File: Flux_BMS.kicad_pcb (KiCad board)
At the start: 4 copper layers, 100 x 100 mm, 151 parts, among them J1 Conn_01x13, J2 CAN, J3 Conn_01x02, J4 Conn_01x05, J5 USB_C_Receptacle_USB2.0, J6 Conn_01x02, J7 Conn_01x05, Q1 BSS84, Q10 BSS84, Q11 BSS84, Q12 BSS84, Q13 Q_NMOS_SDG, Q14 Q_NMOS_SDG, Q2 BSS84, Q3 BSS84, Q4 BSS84, Q5 BSS84, Q6 BSS84, Q7 BSS84, Q8 BSS84, Q9 BSS84, U1 LTC6811-1, U2 STM32L476RGTx, U3 BQ76200PW, U4 TJA1051T-3, U7 SY8502, U8 SE8533, U9 INA180A2, X1 8MHz(16pF)

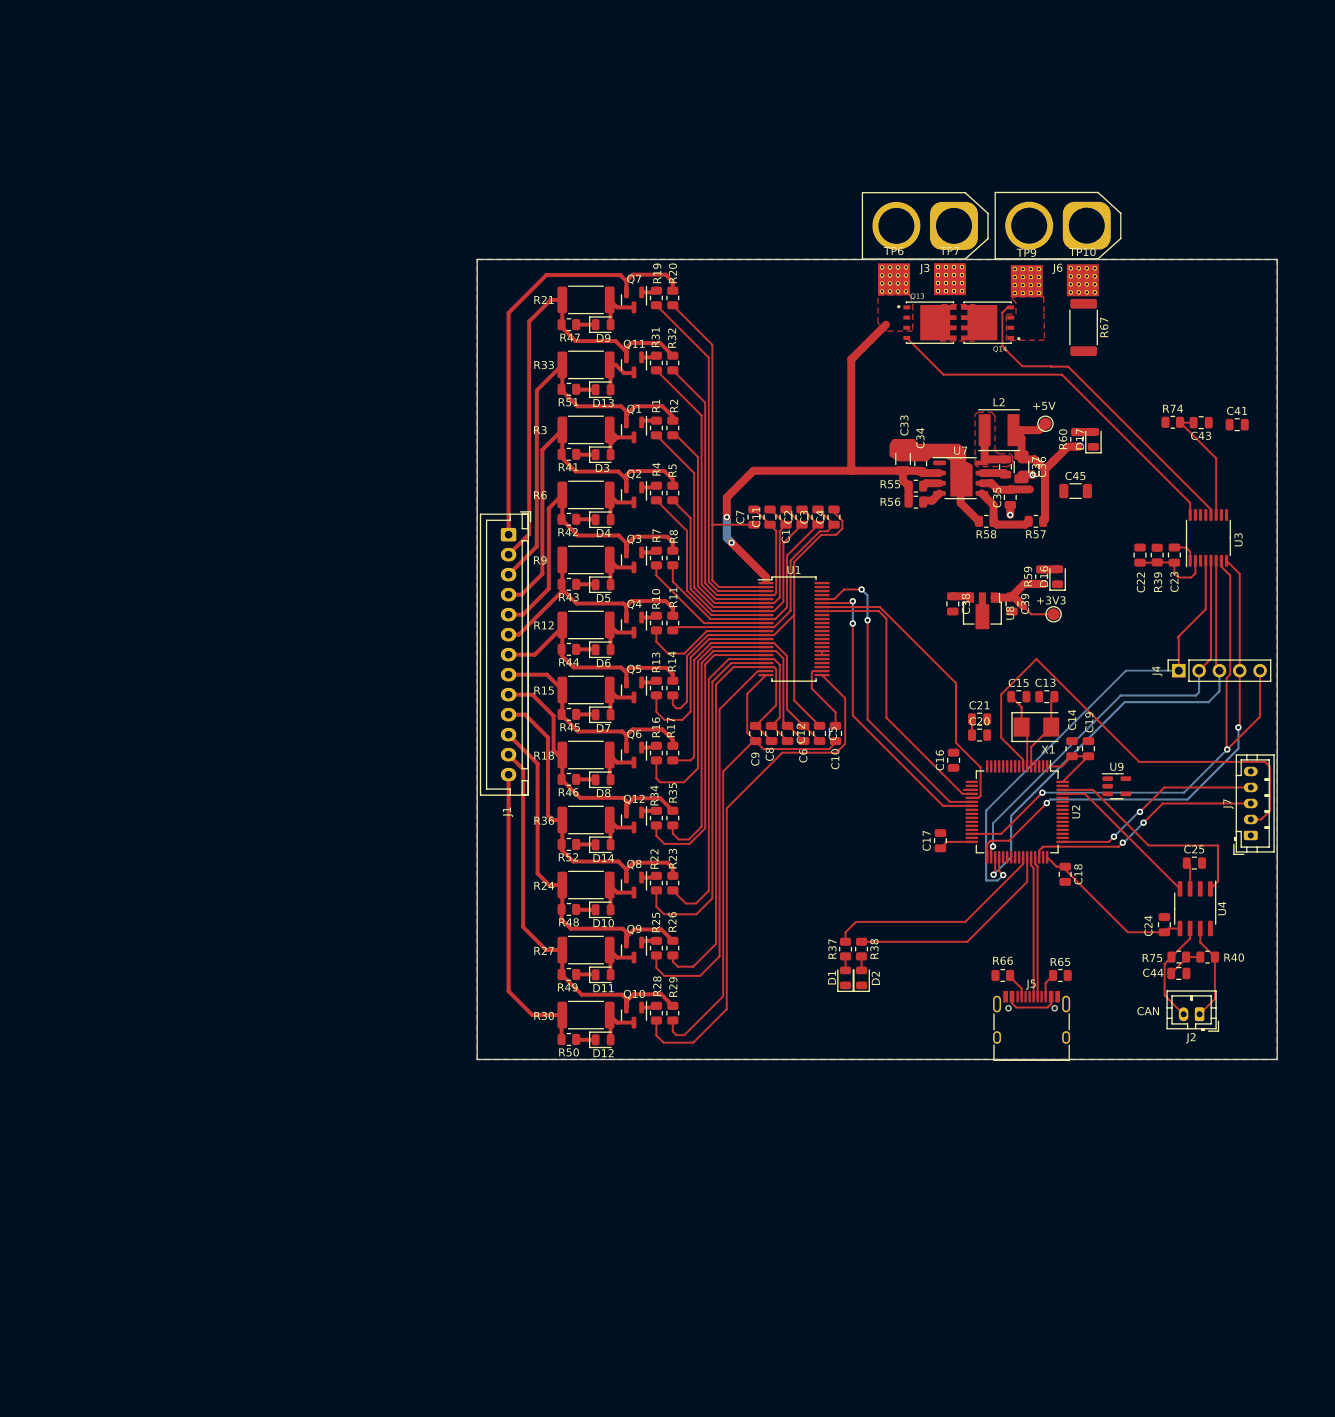
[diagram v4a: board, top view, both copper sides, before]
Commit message: new board dimensions
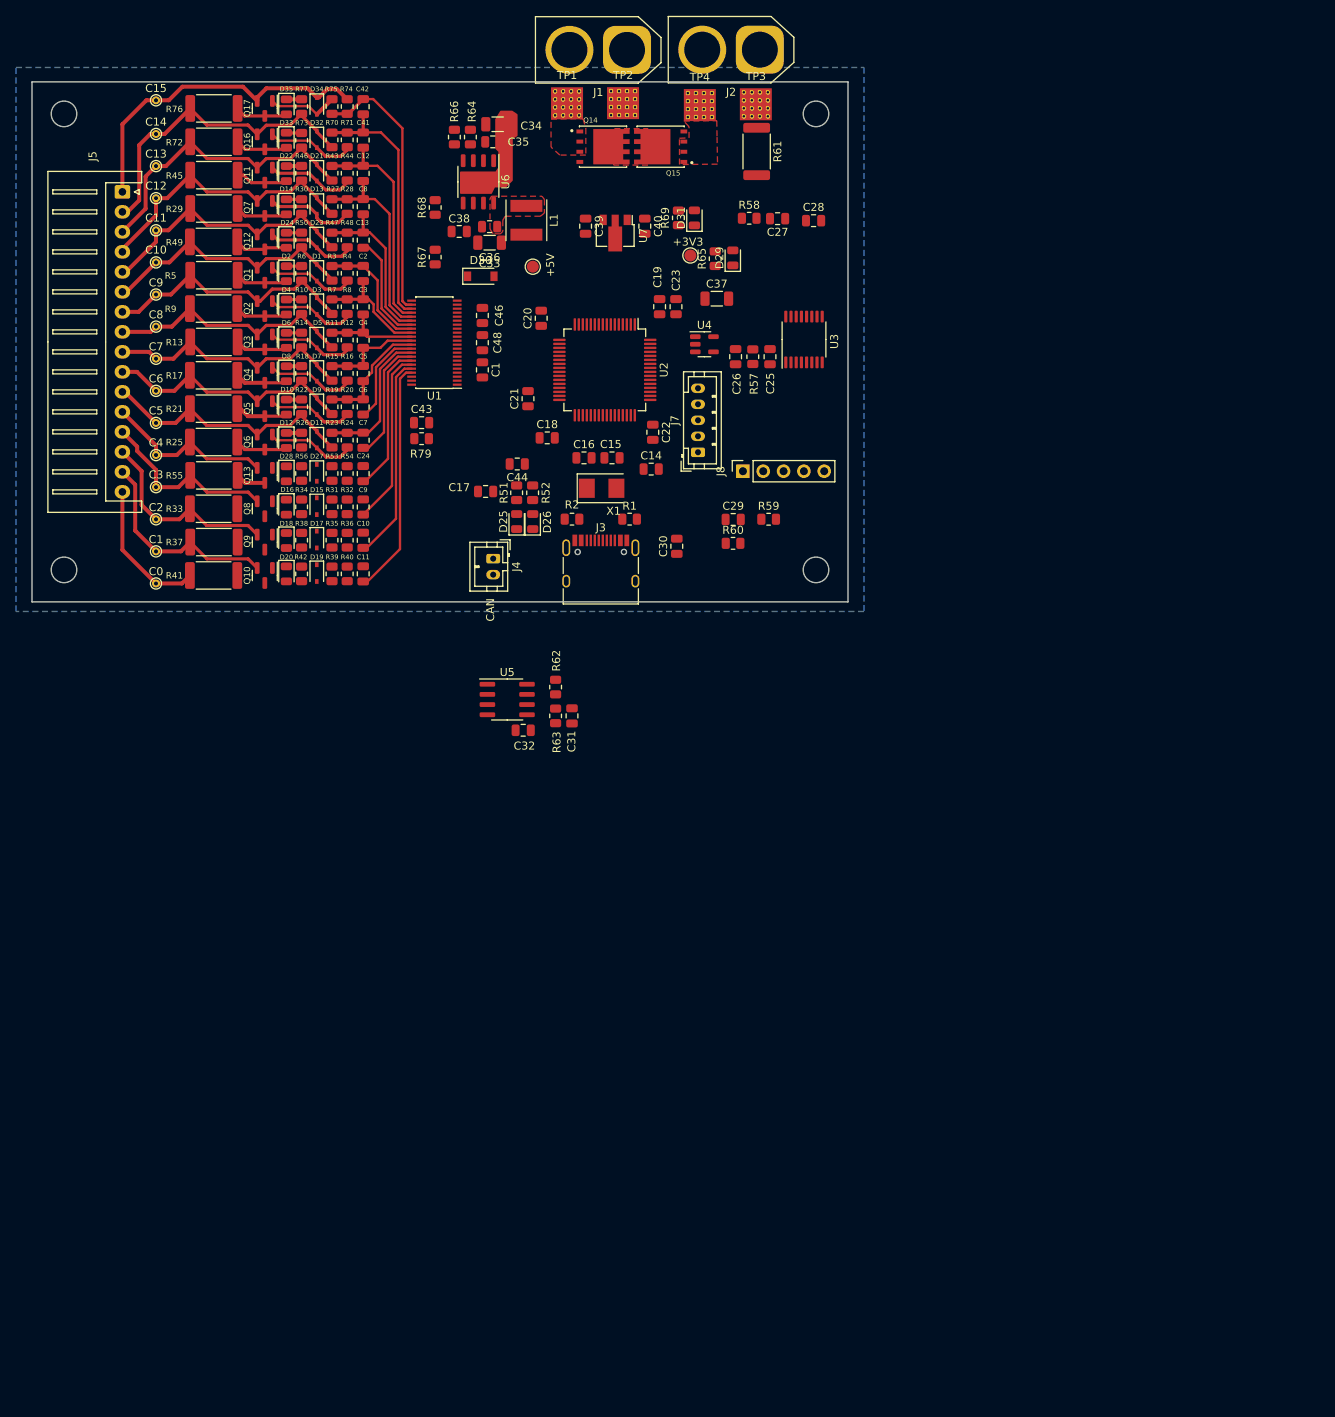
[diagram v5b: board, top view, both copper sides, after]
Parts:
- removed the J1 at (78.9, 84.4)
- removed the R1 at (97.4, 71.1)
- removed the R2 at (99.5, 71.1)
- removed the R51 at (86.5, 66.2)
- removed the R52 at (86.5, 123.1)
- added C13: ~, Capacitor_SMD:C_0805_2012Metric, F.Cu at (60.8, 47.6)
- added C14: C, Capacitor_SMD:C_0805_2012Metric, F.Cu at (96.8, 76.2)
- added C24: ~, Capacitor_SMD:C_0805_2012Metric, F.Cu at (60.8, 76.8)
- added C29: 100n, Capacitor_SMD:C_0805_2012Metric, F.Cu at (107.0, 82.5)
- added C41: ~, Capacitor_SMD:C_0805_2012Metric, F.Cu at (60.8, 35.1)
- added C42: ~, Capacitor_SMD:C_0805_2012Metric, F.Cu at (60.8, 30.9)
- added C43: 470p, Capacitor_SMD:C_0805_2012Metric, F.Cu at (68.0, 70.4)
- added C44: 4u7, Capacitor_SMD:C_0805_2012Metric, F.Cu at (80.0, 75.6)
- added C46: 1u, Capacitor_SMD:C_0805_2012Metric, F.Cu at (75.7, 57.0)
- added C48: 1u, Capacitor_SMD:C_0805_2012Metric, F.Cu at (75.7, 60.4)
- added D1: ~, Diode_SMD:D_SOD-323, F.Cu at (55.0, 51.6)
- added D15: ~, Diode_SMD:D_SOD-323, F.Cu at (55.0, 80.8)
- added D16: RED, LED_SMD:LED_0805_2012Metric, F.Cu at (51.1, 81.0)
- added D17: ~, Diode_SMD:D_SOD-323, F.Cu at (55.0, 85.0)
- added D18: RED, LED_SMD:LED_0805_2012Metric, F.Cu at (51.1, 85.1)
- added D19: ~, Diode_SMD:D_SOD-323, F.Cu at (55.0, 89.2)
- added D2: RED, LED_SMD:LED_0805_2012Metric, F.Cu at (51.1, 51.8)
- added D20: RED, LED_SMD:LED_0805_2012Metric, F.Cu at (51.1, 89.3)
- added D21: ~, Diode_SMD:D_SOD-323, F.Cu at (55.0, 39.1)
- added D22: RED, LED_SMD:LED_0805_2012Metric, F.Cu at (51.1, 39.3)
- added D23: ~, Diode_SMD:D_SOD-323, F.Cu at (55.0, 47.5)
- added D24: RED, LED_SMD:LED_0805_2012Metric, F.Cu at (51.1, 47.6)
- added D27: ~, Diode_SMD:D_SOD-323, F.Cu at (55.0, 76.7)
- added D28: RED, LED_SMD:LED_0805_2012Metric, F.Cu at (51.1, 76.8)
- added D30: D_Schottky, Diode_SMD:D_SOD-123, F.Cu at (75.5, 52.1)
- added D32: ~, Diode_SMD:D_SOD-323, F.Cu at (55.0, 35.0)
- added D33: RED, LED_SMD:LED_0805_2012Metric, F.Cu at (51.1, 35.1)
- added D34: ~, Diode_SMD:D_SOD-323, F.Cu at (55.0, 30.8)
- added D35: RED, LED_SMD:LED_0805_2012Metric, F.Cu at (51.1, 30.9)
- added H1: MountingHole, MountingHole:MountingHole_3.2mm_M3, F.Cu at (23.4, 31.8)
- added H2: MountingHole, MountingHole:MountingHole_3.2mm_M3, F.Cu at (23.4, 88.8)
- added H3: MountingHole, MountingHole:MountingHole_3.2mm_M3, F.Cu at (117.3, 31.8)
- added H4: MountingHole, MountingHole:MountingHole_3.2mm_M3, F.Cu at (117.3, 88.8)
- added J5: Conn_01x16, Connector_JST:JST_XH_S16B-XH-A_1x16_P2.50mm_Horizontal, F.Cu at (30.6, 41.5)
- added Q13: ~, Package_TO_SOT_SMD:SOT-23, F.Cu at (48.5, 77.0)
- added Q16: ~, Package_TO_SOT_SMD:SOT-23, F.Cu at (48.5, 35.3)
- added Q17: ~, Package_TO_SOT_SMD:SOT-23, F.Cu at (48.5, 31.1)
- added R37: 33, Resistor_SMD:R_2512_6332Metric, F.Cu at (42.1, 85.3)
- added R38: 470, Resistor_SMD:R_0805_2012Metric, F.Cu at (53.0, 85.1)
- added R39: 1k, Resistor_SMD:R_0805_2012Metric, F.Cu at (56.9, 89.3)
- added R40: 10k, Resistor_SMD:R_0805_2012Metric, F.Cu at (58.8, 89.3)
- added R53: 1k, Resistor_SMD:R_0805_2012Metric, F.Cu at (56.9, 76.7)
- added R54: 10k, Resistor_SMD:R_0805_2012Metric, F.Cu at (58.8, 76.7)
- added R55: 33, Resistor_SMD:R_2512_6332Metric, F.Cu at (42.1, 77.0)
- added R56: 470, Resistor_SMD:R_0805_2012Metric, F.Cu at (53.0, 76.7)
- added R59: 470k (was 520k), Resistor_SMD:R_0805_2012Metric, F.Cu at (111.4, 82.5)
- added R60: 10k, Resistor_SMD:R_0805_2012Metric, F.Cu at (107.0, 85.5)
- added R70: 1k, Resistor_SMD:R_0805_2012Metric, F.Cu at (56.9, 35.1)
- added R71: 10k, Resistor_SMD:R_0805_2012Metric, F.Cu at (58.8, 35.1)
- added R72: 33, Resistor_SMD:R_2512_6332Metric, F.Cu at (42.1, 35.3)
- added R73: 470, Resistor_SMD:R_0805_2012Metric, F.Cu at (53.0, 35.1)
- added R74: 1k, Resistor_SMD:R_0805_2012Metric, F.Cu at (58.8, 30.9)
- added R75: 10k, Resistor_SMD:R_0805_2012Metric, F.Cu at (56.9, 30.9)
- added R76: 33, Resistor_SMD:R_2512_6332Metric, F.Cu at (42.1, 31.1)
- added R77: 470, Resistor_SMD:R_0805_2012Metric, F.Cu at (53.0, 30.9)
- added R79: 499k, Resistor_SMD:R_0805_2012Metric, F.Cu at (68.0, 72.4)
- added TP10: C12, TestPoint:TestPoint_THTPad_D1.0mm_Drill0.5mm, F.Cu at (34.9, 42.3)
- added TP11: C11, TestPoint:TestPoint_THTPad_D1.0mm_Drill0.5mm, F.Cu at (34.9, 46.4)
- added TP12: C10, TestPoint:TestPoint_THTPad_D1.0mm_Drill0.5mm, F.Cu at (34.9, 50.4)
- added TP13: C9, TestPoint:TestPoint_THTPad_D1.0mm_Drill0.5mm, F.Cu at (34.9, 54.4)
- added TP14: C8, TestPoint:TestPoint_THTPad_D1.0mm_Drill0.5mm, F.Cu at (34.9, 58.4)
- added TP15: C7, TestPoint:TestPoint_THTPad_D1.0mm_Drill0.5mm, F.Cu at (34.9, 62.4)
- added TP16: C6, TestPoint:TestPoint_THTPad_D1.0mm_Drill0.5mm, F.Cu at (34.9, 66.4)
- added TP17: C5, TestPoint:TestPoint_THTPad_D1.0mm_Drill0.5mm, F.Cu at (34.9, 70.4)
- added TP18: C4, TestPoint:TestPoint_THTPad_D1.0mm_Drill0.5mm, F.Cu at (34.9, 74.4)
- added TP19: C3, TestPoint:TestPoint_THTPad_D1.0mm_Drill0.5mm, F.Cu at (34.9, 78.5)
- added TP20: C2, TestPoint:TestPoint_THTPad_D1.0mm_Drill0.5mm, F.Cu at (34.9, 82.5)
- added TP21: C1, TestPoint:TestPoint_THTPad_D1.0mm_Drill0.5mm, F.Cu at (34.9, 86.5)
- added TP22: C0, TestPoint:TestPoint_THTPad_D1.0mm_Drill0.5mm, F.Cu at (34.9, 90.5)
- added TP7: C15, TestPoint:TestPoint_THTPad_D1.0mm_Drill0.5mm, F.Cu at (34.9, 30.1)
- added TP8: C14, TestPoint:TestPoint_THTPad_D1.0mm_Drill0.5mm, F.Cu at (34.9, 34.3)
- added TP9: C13, TestPoint:TestPoint_THTPad_D1.0mm_Drill0.5mm, F.Cu at (34.9, 38.3)
- C1: value 10n -> 1u
- C10, C11, C12, C2, C3, C4, C5, C6, C7, C8, C9: value 10n -> ~
- D11, D13, D3, D5, D7, D9: value RED -> ~; footprint LED_SMD:LED_0805_2012Metric -> Diode_SMD:D_SOD-323
- Q1, Q10, Q11, Q12, Q2, Q3, Q4, Q5, Q6, Q7, Q8, Q9: value BSS84 -> ~
- Q14: renamed from Q13; value Q_NMOS_SDG -> YJG30N06A
- R10, R22, R34: value 3k3 -> 470
- R11, R23, R35: value 100 -> 1k
- R12, R24, R36: value 33 -> 10k; footprint Resistor_SMD:R_2512_6332Metric -> Resistor_SMD:R_0805_2012Metric
- R13, R25: value 3k3 -> 33; footprint Resistor_SMD:R_0805_2012Metric -> Resistor_SMD:R_2512_6332Metric
- R14, R26: value 100 -> 470
- R15, R27, R3: value 33 -> 1k; footprint Resistor_SMD:R_2512_6332Metric -> Resistor_SMD:R_0805_2012Metric
- R16, R28, R4: value 3k3 -> 10k
- R17, R29, R5: value 100 -> 33; footprint Resistor_SMD:R_0805_2012Metric -> Resistor_SMD:R_2512_6332Metric
- R18, R30, R6: value 33 -> 470; footprint Resistor_SMD:R_2512_6332Metric -> Resistor_SMD:R_0805_2012Metric
- R19, R31, R7: value 3k3 -> 1k
- R20, R32, R8: value 100 -> 10k
- R41, R45, R49: value 470 -> 33; footprint Resistor_SMD:R_0805_2012Metric -> Resistor_SMD:R_2512_6332Metric
- R43, R47: value 470 -> 1k
- R44, R48: value 470 -> 10k
- U1: value LTC6811-1 -> BQ76940DBT; footprint Package_SO:SSOP-48_5.3x12.8mm_P0.5mm -> Package_SO:TSSOP-44_4.4x11.2mm_P0.5mm
- moved R29 115.8 mm to (42.1, 43.6), turned to 0 degrees
- moved R28 108.0 mm to (58.8, 43.4), turned to -90 degrees
- moved R30 107.1 mm to (53.0, 43.4), turned to 90 degrees
- moved R50 105.4 mm to (53.0, 47.6), turned to 90 degrees
- moved J4 105.1 mm to (77.0, 87.4), turned to -90 degrees
- moved R49 101.8 mm to (42.0, 47.8)
- moved R27 98.2 mm to (56.9, 43.4), turned to 90 degrees
- moved U5 89.9 mm to (78.8, 105.0), turned to 0 degrees
- moved D14 89.0 mm to (51.1, 43.4), turned to -90 degrees
- moved R62 88.2 mm to (84.8, 103.5), turned to -90 degrees
- moved R48 88.2 mm to (58.8, 47.6), turned to -90 degrees
- moved C12 87.8 mm to (60.8, 39.2)
- moved Q12 85.7 mm to (48.5, 47.8)
- moved D12 84.7 mm to (51.1, 72.6), turned to -90 degrees
- moved J7 84.1 mm to (102.6, 74.1)
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- renumbered C13 to C15, C15 to C16, C20 to C17, C21 to C18, C14 to C19, C16 to C20, C17 to C21, C18 to C22, C19 to C23, C23 to C25, C22 to C26, C43 to C27, C41 to C28, C25 to C30, C44 to C31, C24 to C32, C36 to C33, C33 to C34, C34 to C35, C37 to C36, C45 to C37, C35 to C38, C38 to C39, C39 to C40, D1 to D25, D2 to D26, D17 to D29, D16 to D31, J3 to J1, J6 to J2, J5 to J3, J2 to J4, J4 to J8, L2 to L1, Q14 to Q15, R65 to R1, R66 to R2, R37 to R51, R38 to R52, R39 to R57, R74 to R58, R67 to R61, R40 to R62, R75 to R63, R55 to R64, R60 to R65, R56 to R66, R57 to R67, R58 to R68, R59 to R69, TP6 to TP1, TP7 to TP2, TP10 to TP3, TP9 to TP4, TP1 to TP5, TP8 to TP6, U9 to U4, U4 to U5, U7 to U6, U8 to U7
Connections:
- C1 pad 1: /LTC6811/SENSE+_10 -> Net-(C1-Pad1)
- C1 pad 2: /LTC6811/SENSE+_9 -> GND
- C10 pad 1: /LTC6811/SENSE+_1 -> /BQ76940/SENSE+_2
- C10 pad 2: /LTC6811/Cell1/SENSE- -> /BQ76940/SENSE+_1
- C11 pad 1: /LTC6811/SENSE+_11 -> /BQ76940/SENSE+_1
- C11 pad 2: /LTC6811/SENSE+_10 -> /BQ76940/Cell1/SENSE-
- C12 pad 1: /LTC6811/SENSE+_4 -> /BQ76940/SENSE+_13
- C12 pad 2: /LTC6811/SENSE+_3 -> /BQ76940/SENSE+_12
- C2 pad 1: /LTC6811/SENSE+_9 -> /BQ76940/SENSE+_10
- C2 pad 2: /LTC6811/SENSE+_8 -> /BQ76940/SENSE+_9
- C3 pad 1: /LTC6811/SENSE+_8 -> /BQ76940/SENSE+_9
- C3 pad 2: /LTC6811/SENSE+_7 -> /BQ76940/SENSE+_8
- C4 pad 1: /LTC6811/SENSE+_7 -> /BQ76940/SENSE+_8
- C4 pad 2: /LTC6811/SENSE+_6 -> /BQ76940/SENSE+_7
- C5 pad 1: /LTC6811/SENSE+_6 -> /BQ76940/SENSE+_7
- C5 pad 2: /LTC6811/SENSE+_5 -> /BQ76940/SENSE+_6
- C6 pad 1: /LTC6811/SENSE+_5 -> /BQ76940/SENSE+_6
- C6 pad 2: /LTC6811/SENSE+_4 -> /BQ76940/Cell6/SENSE-
- C7 pad 1: /LTC6811/SENSE+_12 -> /BQ76940/SENSE+_5
- C7 pad 2: /LTC6811/SENSE+_11 -> /BQ76940/SENSE+_4
- C8 pad 1: /LTC6811/SENSE+_3 -> /BQ76940/SENSE+_12
- C8 pad 2: /LTC6811/SENSE+_2 -> /BQ76940/SENSE+_11
- C9 pad 1: /LTC6811/SENSE+_2 -> /BQ76940/SENSE+_3
- C9 pad 2: /LTC6811/SENSE+_1 -> /BQ76940/SENSE+_2
- D11 pad 1: Net-(D11-Pad1) -> /BQ76940/C5
- D13 pad 1: Net-(D13-Pad1) -> /BQ76940/C12
- D3 pad 1: Net-(D3-Pad1) -> /BQ76940/C9
- D5 pad 1: Net-(D5-Pad1) -> /BQ76940/C8
- D7 pad 1: Net-(D7-Pad1) -> /BQ76940/C7
- D9 pad 1: Net-(D9-Pad1) -> /BQ76940/C6
- Q1 pad 1: Net-(Q1-Pad1) -> Net-(D1-Pad2)
- Q1 pad 2: /LTC6811/CELL+_10 -> /BQ76940/C10
- Q1 pad 3: Net-(D3-Pad2) -> Net-(D2-Pad2)
- Q10 pad 1: Net-(Q10-Pad1) -> Net-(D19-Pad2)
- Q10 pad 2: /LTC6811/CELL+_1 -> /BQ76940/C1
- Q10 pad 3: Net-(D12-Pad2) -> Net-(D20-Pad2)
- Q11 pad 1: Net-(Q11-Pad1) -> Net-(D21-Pad2)
- Q11 pad 2: /LTC6811/CELL+_11 -> /BQ76940/C13
- Q11 pad 3: Net-(D13-Pad2) -> Net-(D22-Pad2)
- Q12 pad 1: Net-(Q12-Pad1) -> Net-(D23-Pad2)
- Q12 pad 2: /LTC6811/CELL+_4 -> /BQ76940/C11
- Q12 pad 3: Net-(D14-Pad2) -> Net-(D24-Pad2)
- Q2 pad 1: Net-(Q2-Pad1) -> Net-(D3-Pad2)
- Q2 pad 2: /LTC6811/CELL+_9 -> /BQ76940/C9
- Q3 pad 1: Net-(Q3-Pad1) -> Net-(D5-Pad2)
- Q3 pad 2: /LTC6811/CELL+_8 -> /BQ76940/C8
- Q3 pad 3: Net-(D5-Pad2) -> Net-(D6-Pad2)
- Q4 pad 1: Net-(Q4-Pad1) -> Net-(D7-Pad2)
- Q4 pad 2: /LTC6811/CELL+_7 -> /BQ76940/C7
- Q4 pad 3: Net-(D6-Pad2) -> Net-(D8-Pad2)
- Q5 pad 1: Net-(Q5-Pad1) -> Net-(D9-Pad2)
- Q5 pad 2: /LTC6811/CELL+_6 -> /BQ76940/C6
- Q5 pad 3: Net-(D7-Pad2) -> Net-(D10-Pad2)
- Q6 pad 1: Net-(Q6-Pad1) -> Net-(D11-Pad2)
- Q6 pad 2: /LTC6811/CELL+_5 -> /BQ76940/C5
- Q6 pad 3: Net-(D8-Pad2) -> Net-(D12-Pad2)
- Q7 pad 1: Net-(Q7-Pad1) -> Net-(D13-Pad2)
- Q7 pad 2: /LTC6811/CELL+_12 -> /BQ76940/C12
- Q7 pad 3: Net-(D9-Pad2) -> Net-(D14-Pad2)
- Q8 pad 1: Net-(Q8-Pad1) -> Net-(D15-Pad2)
- Q8 pad 2: /LTC6811/CELL+_3 -> /BQ76940/C3
- Q8 pad 3: Net-(D10-Pad2) -> Net-(D16-Pad2)
- Q9 pad 1: Net-(Q9-Pad1) -> Net-(D17-Pad2)
- Q9 pad 2: /LTC6811/CELL+_2 -> /BQ76940/C2
- Q9 pad 3: Net-(D11-Pad2) -> Net-(D18-Pad2)
- R10 pad 1: /LTC6811/BALANCE_7 -> /BQ76940/C8
- R10 pad 2: Net-(Q4-Pad1) -> Net-(D4-Pad1)
- R11 pad 1: /LTC6811/CELL+_7 -> /BQ76940/C8
- R11 pad 2: /LTC6811/SENSE+_7 -> /BQ76940/SENSE+_8
- R12 pad 1: /LTC6811/CELL+_6 -> /BQ76940/SENSE+_8
- R12 pad 2: Net-(D6-Pad2) -> Net-(D5-Pad2)
- R13 pad 1: /LTC6811/BALANCE_6 -> /BQ76940/C7
- R13 pad 2: Net-(Q5-Pad1) -> Net-(D6-Pad2)
- R14 pad 1: /LTC6811/CELL+_6 -> /BQ76940/C7
- R14 pad 2: /LTC6811/SENSE+_6 -> Net-(D6-Pad1)
- R15 pad 1: /LTC6811/CELL+_5 -> /BQ76940/C7
- R15 pad 2: Net-(D7-Pad2) -> /BQ76940/SENSE+_7
- R16 pad 1: /LTC6811/BALANCE_5 -> /BQ76940/SENSE+_7
- R16 pad 2: Net-(Q6-Pad1) -> Net-(D7-Pad2)
- R17 pad 1: /LTC6811/CELL+_5 -> /BQ76940/C6
- R17 pad 2: /LTC6811/SENSE+_5 -> Net-(D8-Pad2)
- R18 pad 1: /LTC6811/CELL+_4 -> /BQ76940/C6
- R18 pad 2: Net-(D8-Pad2) -> Net-(D8-Pad1)
- R19 pad 1: /LTC6811/BALANCE_12 -> /BQ76940/C6
- R19 pad 2: Net-(Q7-Pad1) -> /BQ76940/SENSE+_6
- R20 pad 1: /LTC6811/CELL+_12 -> /BQ76940/SENSE+_6
- R20 pad 2: /LTC6811/SENSE+_12 -> Net-(D9-Pad2)
- R21 pad 1: /LTC6811/CELL+_11 -> /BQ76940/C5
- R21 pad 2: Net-(D9-Pad2) -> Net-(D10-Pad2)
- R22 pad 1: /LTC6811/BALANCE_3 -> /BQ76940/C5
- R22 pad 2: Net-(Q8-Pad1) -> Net-(D10-Pad1)
- R23 pad 1: /LTC6811/CELL+_3 -> /BQ76940/C5
- R23 pad 2: /LTC6811/SENSE+_3 -> /BQ76940/SENSE+_5
- R24 pad 1: /LTC6811/CELL+_2 -> /BQ76940/SENSE+_5
- R24 pad 2: Net-(D10-Pad2) -> Net-(D11-Pad2)
- R25 pad 1: /LTC6811/BALANCE_2 -> /BQ76940/C4
- R25 pad 2: Net-(Q9-Pad1) -> Net-(D12-Pad2)
- R26 pad 1: /LTC6811/CELL+_2 -> /BQ76940/C4
- R26 pad 2: /LTC6811/SENSE+_2 -> Net-(D12-Pad1)
- R27 pad 1: /LTC6811/CELL+_1 -> /BQ76940/C12
- R27 pad 2: Net-(D11-Pad2) -> /BQ76940/SENSE+_12
- R28 pad 1: /LTC6811/BALANCE_1 -> /BQ76940/SENSE+_12
- R28 pad 2: Net-(Q10-Pad1) -> Net-(D13-Pad2)
- R29 pad 1: /LTC6811/CELL+_1 -> /BQ76940/C11
- R29 pad 2: /LTC6811/SENSE+_1 -> Net-(D14-Pad2)
- R3 pad 1: /LTC6811/CELL+_9 -> /BQ76940/C10
- R3 pad 2: Net-(D3-Pad2) -> /BQ76940/SENSE+_10
- R30 pad 1: /LTC6811/CELL-_1 -> /BQ76940/C11
- R30 pad 2: Net-(D12-Pad2) -> Net-(D14-Pad1)
- R31 pad 1: /LTC6811/BALANCE_11 -> /BQ76940/C3
- R31 pad 2: Net-(Q11-Pad1) -> /BQ76940/SENSE+_3
- R32 pad 1: /LTC6811/CELL+_11 -> /BQ76940/SENSE+_3
- R32 pad 2: /LTC6811/SENSE+_11 -> Net-(D15-Pad2)
- R33 pad 1: /LTC6811/CELL+_10 -> /BQ76940/C2
- R33 pad 2: Net-(D13-Pad2) -> Net-(D16-Pad2)
- R34 pad 1: /LTC6811/BALANCE_4 -> /BQ76940/C2
- R34 pad 2: Net-(Q12-Pad1) -> Net-(D16-Pad1)
- R35 pad 1: /LTC6811/CELL+_4 -> /BQ76940/C2
- R35 pad 2: /LTC6811/SENSE+_4 -> /BQ76940/SENSE+_2
- R36 pad 1: /LTC6811/CELL+_3 -> /BQ76940/SENSE+_2
- R36 pad 2: Net-(D14-Pad2) -> Net-(D17-Pad2)
- R4 pad 1: /LTC6811/BALANCE_9 -> /BQ76940/SENSE+_10
- R4 pad 2: Net-(Q2-Pad1) -> Net-(D1-Pad2)
- R41 pad 1: /LTC6811/CELL+_9 -> /BQ76940/C0
- R41 pad 2: Net-(D3-Pad1) -> Net-(D20-Pad2)
- R42 pad 1: /LTC6811/CELL+_8 -> /BQ76940/C0
- R42 pad 2: Net-(D4-Pad1) -> Net-(D20-Pad1)
- R43 pad 1: /LTC6811/CELL+_7 -> /BQ76940/C13
- R43 pad 2: Net-(D5-Pad1) -> /BQ76940/SENSE+_13
- R44 pad 1: /LTC6811/CELL+_6 -> /BQ76940/SENSE+_13
- R44 pad 2: Net-(D6-Pad1) -> Net-(D21-Pad2)
- R45 pad 1: /LTC6811/CELL+_5 -> /BQ76940/C12
- R45 pad 2: Net-(D7-Pad1) -> Net-(D22-Pad2)
- R46 pad 1: /LTC6811/CELL+_4 -> /BQ76940/C12
- R46 pad 2: Net-(D8-Pad1) -> Net-(D22-Pad1)
- R47 pad 1: /LTC6811/CELL+_11 -> /BQ76940/C11
- R47 pad 2: Net-(D9-Pad1) -> /BQ76940/SENSE+_11
- R48 pad 1: /LTC6811/CELL+_2 -> /BQ76940/SENSE+_11
- R48 pad 2: Net-(D10-Pad1) -> Net-(D23-Pad2)
- R49 pad 1: /LTC6811/CELL+_1 -> /BQ76940/C10
- R49 pad 2: Net-(D11-Pad1) -> Net-(D24-Pad2)
- R5 pad 1: /LTC6811/CELL+_9 -> /BQ76940/C9
- R5 pad 2: /LTC6811/SENSE+_9 -> Net-(D2-Pad2)
- R50 pad 1: /LTC6811/CELL-_1 -> /BQ76940/C10
- R50 pad 2: Net-(D12-Pad1) -> Net-(D24-Pad1)
- R6 pad 1: /LTC6811/CELL+_8 -> /BQ76940/C9
- R6 pad 2: Net-(D4-Pad2) -> Net-(D2-Pad1)
- R7 pad 1: /LTC6811/BALANCE_8 -> /BQ76940/C9
- R7 pad 2: Net-(Q3-Pad1) -> /BQ76940/SENSE+_9
- R8 pad 1: /LTC6811/CELL+_8 -> /BQ76940/SENSE+_9
- R8 pad 2: /LTC6811/SENSE+_8 -> Net-(D3-Pad2)
- R9 pad 1: /LTC6811/CELL+_7 -> /BQ76940/C8
- R9 pad 2: Net-(D5-Pad2) -> Net-(D4-Pad2)
- U1 pad 1: V+ -> unconnected-(U1-Pad1)
- U1 pad 10: /LTC6811/SENSE+_8 -> /BQ76940/VC5X
- U1 pad 11: /LTC6811/BALANCE_8 -> Net-(C48-Pad2)
- U1 pad 12: /LTC6811/SENSE+_7 -> Net-(C48-Pad2)
- U1 pad 13: /LTC6811/BALANCE_7 -> /BQ76940/TS2
- U1 pad 14: /LTC6811/SENSE+_6 -> Net-(C48-Pad2)
- U1 pad 15: /LTC6811/BALANCE_6 -> /BQ76940/VC10X
- U1 pad 16: /LTC6811/SENSE+_5 -> Net-(C46-Pad2)
- U1 pad 17: /LTC6811/BALANCE_5 -> Net-(C46-Pad2)
- U1 pad 18: /LTC6811/SENSE+_4 -> /BQ76940/TS3
- U1 pad 19: /LTC6811/BALANCE_4 -> Net-(C46-Pad2)
- U1 pad 2: /LTC6811/SENSE+_12 -> unconnected-(U1-Pad2)
- U1 pad 20: /LTC6811/SENSE+_3 -> /BQ76940/BAT
- U1 pad 21: /LTC6811/BALANCE_3 -> unconnected-(U1-Pad21)
- U1 pad 22: /LTC6811/SENSE+_2 -> unconnected-(U1-Pad22)
- U1 pad 23: /LTC6811/BALANCE_2 -> unconnected-(U1-Pad23)
- U1 pad 24: /LTC6811/SENSE+_1 -> /BQ76940/SENSE+_15
- U1 pad 25: /LTC6811/BALANCE_1 -> /BQ76940/SENSE+_14
- U1 pad 26: /LTC6811/Cell1/SENSE- -> /BQ76940/SENSE+_13
- U1 pad 27: unconnected-(U1-Pad27) -> /BQ76940/SENSE+_12
- U1 pad 28: unconnected-(U1-Pad28) -> /BQ76940/SENSE+_11
- U1 pad 29: unconnected-(U1-Pad29) -> /BQ76940/Cell11/SENSE-
- U1 pad 3: /LTC6811/BALANCE_12 -> GND
- U1 pad 30: V- -> /BQ76940/SENSE+_10
- U1 pad 31: V- -> /BQ76940/SENSE+_9
- U1 pad 32: unconnected-(U1-Pad32) -> /BQ76940/SENSE+_8
- U1 pad 33: unconnected-(U1-Pad33) -> /BQ76940/SENSE+_7
- U1 pad 34: unconnected-(U1-Pad34) -> /BQ76940/SENSE+_6
- U1 pad 35: unconnected-(U1-Pad35) -> /BQ76940/Cell6/SENSE-
- U1 pad 36: unconnected-(U1-Pad36) -> /BQ76940/SENSE+_5
- U1 pad 37: unconnected-(U1-Pad37) -> /BQ76940/SENSE+_4
- U1 pad 38: unconnected-(U1-Pad38) -> /BQ76940/SENSE+_3
- U1 pad 39: unconnected-(U1-Pad39) -> /BQ76940/SENSE+_2
- U1 pad 4: /LTC6811/SENSE+_11 -> /BQ76940/BQ_SDA
- U1 pad 40: unconnected-(U1-Pad40) -> /BQ76940/SENSE+_1
- U1 pad 41: /LTC6811/LTC_CS -> /BQ76940/Cell1/SENSE-
- U1 pad 42: /LTC6811/LTC_SCK -> unconnected-(U1-Pad42)
- U1 pad 43: /LTC6811/LTC_SDI -> unconnected-(U1-Pad43)
- U1 pad 44: /LTC6811/LTC_SDO -> /BQ76940/BQ_ALERT
- U1 pad 5: /LTC6811/BALANCE_11 -> /BQ76940/BQ_SCL
- U1 pad 6: /LTC6811/SENSE+_10 -> /BQ76940/TS1
- U1 pad 7: /LTC6811/BALANCE_10 -> Net-(C1-Pad1)
- U1 pad 8: /LTC6811/SENSE+_9 -> Net-(C44-Pad1)
- U1 pad 9: /LTC6811/BALANCE_9 -> unconnected-(U1-Pad9)
- U2 pad 20: /LTC6811/LTC_CS -> /STM32L476/LTC_CS
- U2 pad 21: /LTC6811/LTC_SCK -> /STM32L476/LTC_SCK
- U2 pad 22: /LTC6811/LTC_SDO -> /STM32L476/LTC_SDO
- U2 pad 23: /LTC6811/LTC_SDI -> /STM32L476/LTC_SDI
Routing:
- net /Charge_control/BQ_PMON_EN: track 72.1 -> 0.00 mm, vias 2 -> 0
- net /LTC6811/BALANCE_1: track 65.8 -> 0.00 mm
- net V+: track 64.5 -> 0.00 mm, vias 2 -> 0
- net /LTC6811/SENSE+_1: track 64.2 -> 0.00 mm
- net /Charge_control/BQ_PCHG_EN: track 62.2 -> 0.00 mm, vias 2 -> 0
- net /Charge_control/BQ_CHG_EN: track 60.2 -> 0.00 mm, vias 1 -> 0
- net /STM32L476/NRST: track 59.5 -> 0.00 mm
- net /Charge_control/BQ_DSG_EN: track 59.5 -> 0.00 mm, vias 1 -> 0
- net /LTC6811/SENSE+_2: track 59.5 -> 0.00 mm
- net /LTC6811/SENSE+_6: track 57.1 -> 0.00 mm
- net /LTC6811/CELL+_11: track 56.9 -> 0.00 mm
- net /Charge_control/BQ_CP_EN: track 53.9 -> 0.00 mm, vias 1 -> 0
- net /LTC6811/CELL+_12: track 53.7 -> 0.00 mm
- net /LTC6811/SENSE+_3: track 53.3 -> 0.00 mm
- net /LTC6811/CELL+_10: track 50.1 -> 0.00 mm
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- removed copper zone on F.Cu, net GND
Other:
- board size 100 x 100 mm -> 102 x 65 mm

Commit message: placed bleed resistors
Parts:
- removed C33, C38, C39: 1u, Capacitor_SMD:C_0805_2012Metric
- removed C34: 2.2u/100V, Capacitor_SMD:C_1206_3216Metric
- removed C35: 220n, Capacitor_SMD:C_0805_2012Metric
- removed C36, C37: 22u, Capacitor_SMD:C_1206_3216Metric
- removed C40: 10u, Capacitor_SMD:C_0805_2012Metric
- removed D29, D31: RED, LED_SMD:LED_0805_2012Metric
- removed D30: D_Schottky, Diode_SMD:D_SOD-123
- removed L1: 47u, Inductor_SMD:L_Taiyo-Yuden_NR-50xx
- removed R64, R67: 100k, Resistor_SMD:R_0805_2012Metric
- removed R65, R69: 1k, Resistor_SMD:R_0805_2012Metric
- removed R66: 1.6M, Resistor_SMD:R_0805_2012Metric
- removed R68: 31k6, Resistor_SMD:R_0805_2012Metric
- removed TP5: +5V, TestPoint:TestPoint_Pad_D1.5mm
- removed TP6: +3V3, TestPoint:TestPoint_Pad_D1.5mm
- removed U6: SY8502, Package_SO:HSOP-8-1EP_3.9x4.9mm_P1.27mm_EP2.41x3.1mm
- removed U7: SE8533, Package_TO_SOT_SMD:SOT-89-3
- added C50: 2n2, Capacitor_SMD:C_0805_2012Metric, F.Cu at (124.2, 87.6)
- added C52: 2u2/100V, Capacitor_SMD:C_1206_3216Metric, F.Cu at (123.2, 76.6)
- added C53: 22u, Capacitor_SMD:C_1210_3225Metric, F.Cu at (119.5, 90.9)
- added C54: 10u, Capacitor_SMD:C_0805_2012Metric, F.Cu at (122.2, 92.2)
- added C55: 10u, Capacitor_SMD:C_0805_2012Metric, F.Cu at (129.2, 93.8)
- added L2: 33u, Inductor_SMD:L_Taiyo-Yuden_NR-80xx, F.Cu at (130.4, 84.3)
- added R83: 316k, Resistor_SMD:R_0805_2012Metric, F.Cu at (119.7, 81.3)
- added R84: 101k, Resistor_SMD:R_0805_2012Metric, F.Cu at (119.5, 85.1)
- added R85: 41k2, Resistor_SMD:R_0805_2012Metric, F.Cu at (121.2, 77.2)
- added U8: ME6118A33, Package_TO_SOT_SMD:SOT-89-3, F.Cu at (125.7, 93.0)
- added U9: LM5164DDA, Package_SO:HSOP-8-1EP_3.9x4.9mm_P1.27mm_EP2.41x3.1mm_ThermalVias, F.Cu at (123.3, 82.9)
- moved J4 94.6 mm to (158.3, 135.7), turned to 0 degrees
- moved R63 72.2 mm to (151.8, 134.1)
- moved C31 72.2 mm to (153.8, 134.1)
- moved C32 72.2 mm to (147.8, 135.8)
- moved R62 72.2 mm to (151.8, 130.4)
- moved U5 72.2 mm to (145.8, 132.0)
- moved C15 69.2 mm to (143.7, 120.7)
- moved C16 69.2 mm to (140.2, 120.7)
- moved C18 69.2 mm to (135.6, 118.2)
- moved C20 69.2 mm to (134.8, 103.2)
- moved C23 69.2 mm to (151.7, 101.8)
- moved D10 69.2 mm to (103.0, 114.3)
- moved D16 69.2 mm to (103.0, 126.9)
- moved D18 69.2 mm to (103.0, 131.0)
- moved D2 69.2 mm to (103.0, 97.7)
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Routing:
- removed copper zone on F.Cu, net Net-(C33-Pad2)

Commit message: before meeting
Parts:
- added C33: 1u, Capacitor_SMD:C_0805_2012Metric, F.Cu at (137.8, 99.4)
- added C34: 1u, Capacitor_SMD:C_0805_2012Metric, F.Cu at (141.1, 102.6)
- added C45: 4u7, Capacitor_SMD:C_0805_2012Metric, F.Cu at (126.8, 102.0)
- added C47: 4u7, Capacitor_SMD:C_0805_2012Metric, F.Cu at (126.8, 106.3)
- added C49: 4u7, Capacitor_SMD:C_0805_2012Metric, F.Cu at (128.8, 112.6)
- added Q18: BST82,215, Package_TO_SOT_SMD:SOT-23, F.Cu at (137.8, 102.7)
- added R64: 100k, Resistor_SMD:R_0805_2012Metric, F.Cu at (121.8, 99.1)
- added R65: 1k, Resistor_SMD:R_0805_2012Metric, F.Cu at (125.5, 99.1)
- added R66: 100k, Resistor_SMD:R_0805_2012Metric, F.Cu at (133.1, 106.2)
- added R78: 1k, Resistor_SMD:R_0805_2012Metric, F.Cu at (119.3, 90.6)
- added R80: 10k, Resistor_SMD:R_0805_2012Metric, F.Cu at (128.8, 102.0)
- added R81: 10k, Resistor_SMD:R_0805_2012Metric, F.Cu at (128.8, 106.3)
- added R82: 10k, Resistor_SMD:R_0805_2012Metric, F.Cu at (126.8, 112.6)
- added U6: USBLC6-2SC6, Package_TO_SOT_SMD:SOT-23-6, F.Cu at (124.5, 127.1)
- moved J8 27.0 mm to (159.5, 95.3), turned to 0 degrees
- moved C28 25.5 mm to (144.4, 98.3)
- moved U3 22.9 mm to (155.2, 86.7)
- moved C25 22.7 mm to (151.1, 89.0)
- moved C26 22.7 mm to (146.8, 89.0)
- moved R57 22.7 mm to (148.9, 89.0)
- moved C27 22.4 mm to (142.6, 95.8)
- moved R58 18.5 mm to (142.4, 93.2), turned to 180 degrees
- moved Q15 16.1 mm to (133.7, 81.8)
- moved Q14 16.1 mm to (126.5, 81.8)
- moved C32 15.8 mm to (131.9, 136.6), turned to 90 degrees
- moved C55 15.5 mm to (144.1, 89.1)
- moved C54 15.3 mm to (136.4, 86.7), turned to 90 degrees
- moved J1 15.3 mm to (130.2, 69.7)
- moved R61 15.3 mm to (146.4, 82.4)
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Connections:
- J3 pad A6: /STM32L476/USB_DP -> Net-(J3-PadA6)
- J3 pad A7: /STM32L476/USB_DM -> Net-(J3-PadA7)
- J3 pad B6: /STM32L476/USB_DP -> Net-(J3-PadA6)
- J3 pad B7: /STM32L476/USB_DM -> Net-(J3-PadA7)
- U1 pad 42: unconnected-(U1-Pad42) -> GND
- U1 pad 43: unconnected-(U1-Pad43) -> GND
- U1 pad 9: unconnected-(U1-Pad9) -> Net-(U1-Pad9)
- U4 pad 5: (no net) -> +3V3
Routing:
- net /BQ76940/C0: track 17.8 -> 33.3 mm
- net /BQ76940/C4: track 21.8 -> 34.3 mm
- net /BQ76940/C1: track 26.1 -> 38.5 mm
- net /BQ76940/C2: track 24.7 -> 37.1 mm
- net /BQ76940/C3: track 23.2 -> 35.6 mm
- net Net-(D17-Pad2): track 0.00 -> 11.2 mm
- net Net-(D27-Pad2): track 0.00 -> 11.0 mm
- net Net-(D19-Pad2): track 0.00 -> 11.0 mm
- net Net-(D15-Pad2): track 0.00 -> 11.0 mm
- net Net-(D20-Pad2): track 0.00 -> 6.65 mm
- net Net-(D18-Pad2): track 0.00 -> 6.61 mm
- net Net-(D16-Pad2): track 0.00 -> 6.61 mm
- net /BQ76940/SENSE+_1: track 25.7 -> 31.9 mm
- net /BQ76940/SENSE+_4: track 15.3 -> 21.5 mm
- net /BQ76940/SENSE+_3: track 18.6 -> 24.8 mm
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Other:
- board size 102 x 65 mm -> 90 x 65 mm
